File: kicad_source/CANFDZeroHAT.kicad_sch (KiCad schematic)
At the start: 34 parts, among them CN1 RASPI-IO, CN2 691322310004, CN3 GH_SM04B-GHS-TB, CN4 GH_SM04B-GHS-TB, SW1 JS202011JCQN, U1 MCP2518FD, U2 TCAN332GDR, Y1 RH100-40.000-18-F-2050-TR

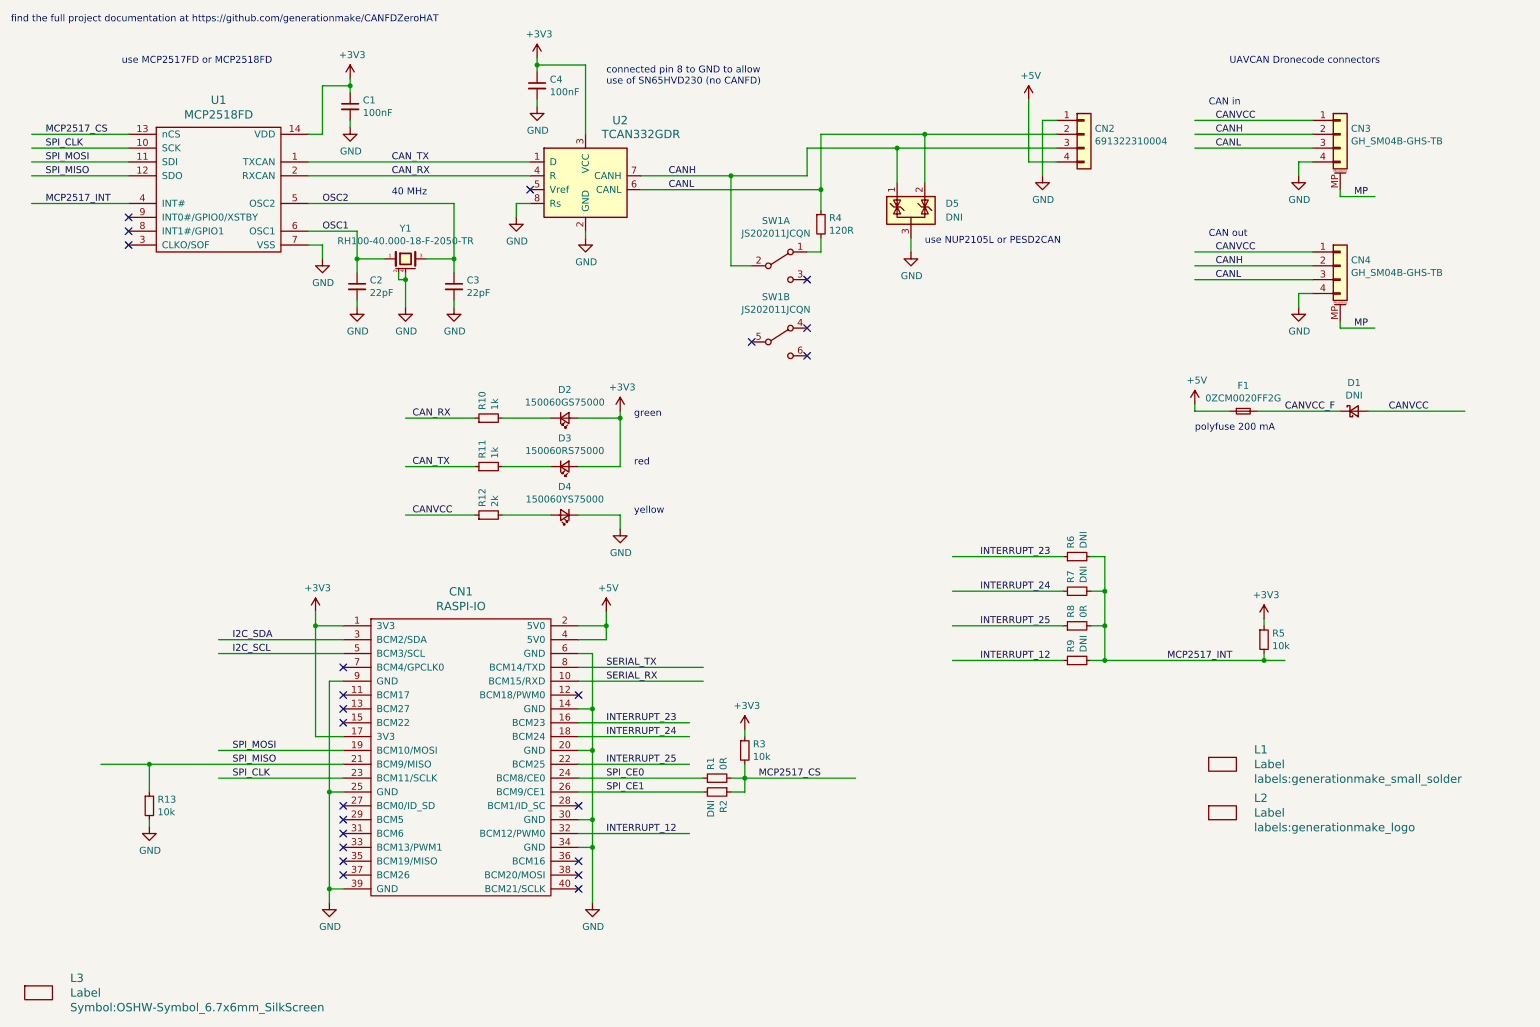
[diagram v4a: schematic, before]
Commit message: added some JLCPCB part numbers
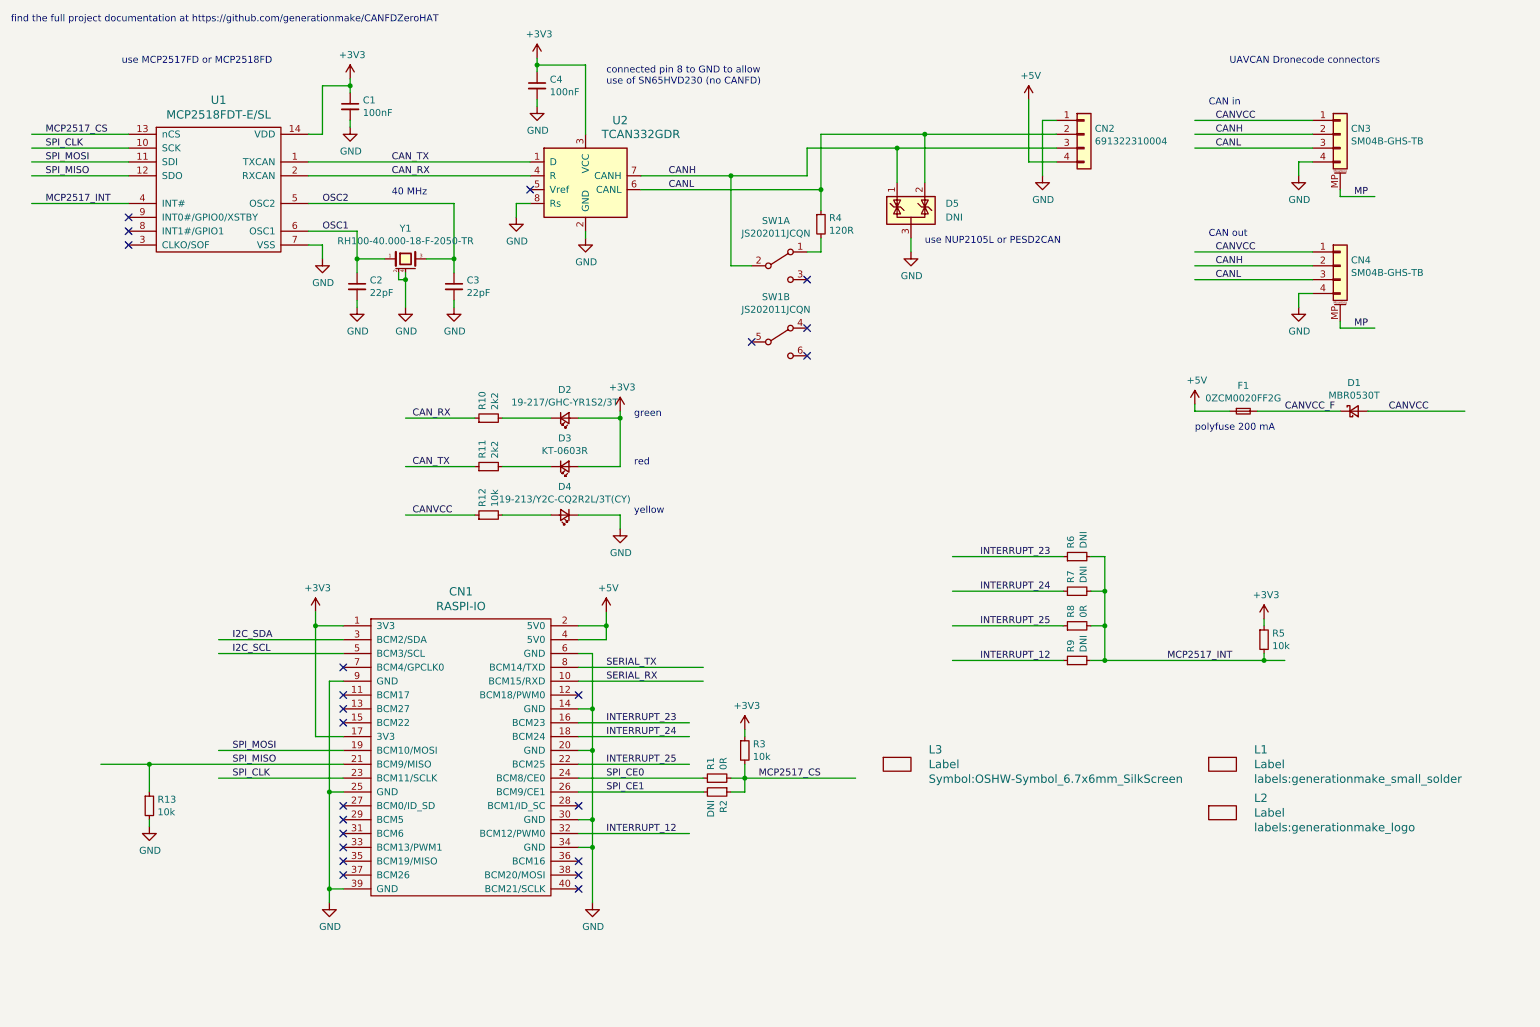
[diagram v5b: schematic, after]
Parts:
- C1, C4: LCSC (none) -> C14663
- C2, C3, D5, L1, L2, L3, R2, R6, R7, R9: now left out of the parts list
- CN3, CN4: value GH_SM04B-GHS-TB -> SM04B-GHS-TB; LCSC (none) -> C189895
- D1: value DNI -> MBR0530T; LCSC (none) -> C77336
- D2: value 150060GS75000 -> 19-217/GHC-YR1S2/3T; LCSC (none) -> C72043
- D3: value 150060RS75000 -> KT-0603R; LCSC (none) -> C2286
- D4: value 150060YS75000 -> 19-213/Y2C-CQ2R2L/3T(CY); LCSC (none) -> C72038
- R1, R8: LCSC (none) -> C2889381
- R10, R11: value 1k -> 2k2; LCSC (none) -> C4190
- R12: value 2k -> 10k; LCSC (none) -> C25804
- R13, R3, R5: LCSC (none) -> C25804
- R4: LCSC (none) -> C22787
- U1: value MCP2518FD -> MCP2518FDT-E/SL; LCSC (none) -> C626758
- U2: LCSC (none) -> C191010
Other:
- moved on the sheet: L3

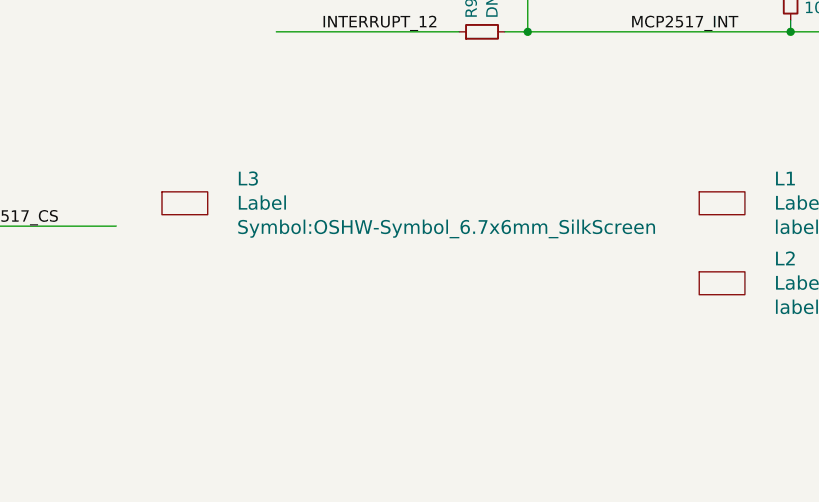
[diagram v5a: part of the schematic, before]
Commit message: added cyphal logo
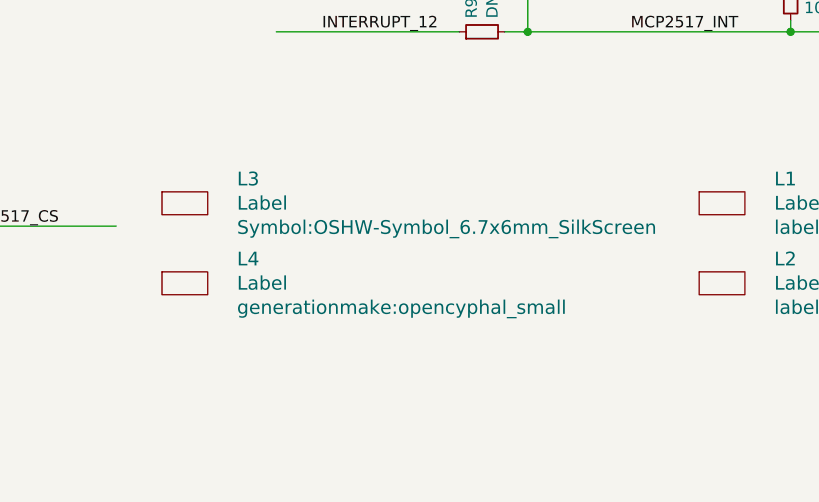
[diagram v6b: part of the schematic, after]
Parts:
- added L4: Label, generationmake:opencyphal_small, symbol generationmake:Label
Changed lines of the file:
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@@
   (title_block
     (title "CANFDZeroHAT")
-    (date "2023-08-24")
+    (date "2023-08-27")
     (rev "0.3")
     (company "generationmake")
@@
     (pin "2")
   )
+  (symbol (lib_id "generationmake:Label") (at 175.26 160.02 0) (unit 1)
+    (in_bom no) (on_board yes)
+    (property "Reference" "L4" (id 0) (at 181.0512 157.3276 0)
+      (effects (font (size 1.524 1.524)) (justify left))
+    )
+    (property "Value" "Label" (id 1) (at 181.0512 160.02 0)
+      (effects (font (size 1.524 1.524)) (justify left))
+    )
+    (property "Footprint" "generationmake:opencyphal_small" (id 2) (at 181.0512 162.7124 0)
+      (effects (font (size 1.524 1.524)) (justify left))
+    )
+    (property "Datasheet" "" (id 3) (at 175.26 160.02 0)
+      (effects (font (size 1.524 1.524)))
+    )
+  )
   (symbol (lib_id "Switch:SW_DPDT_x2") (at 153.67 73.66 0) (unit 2)
     (in_bom yes) (on_board yes)
@@
       (reference "L3") (unit 1) (value "Label") (footprint "Symbol:OSHW-Symbol_6.7x6mm_SilkScreen")
     )
+    (path "/c90de6ec-8b1e-4482-a692-291e6d522cdb"
+      (reference "L4") (unit 1) (value "Label") (footprint "generationmake:opencyphal_small")
+    )
     (path "/00000000-0000-0000-0000-00005fd836f1"

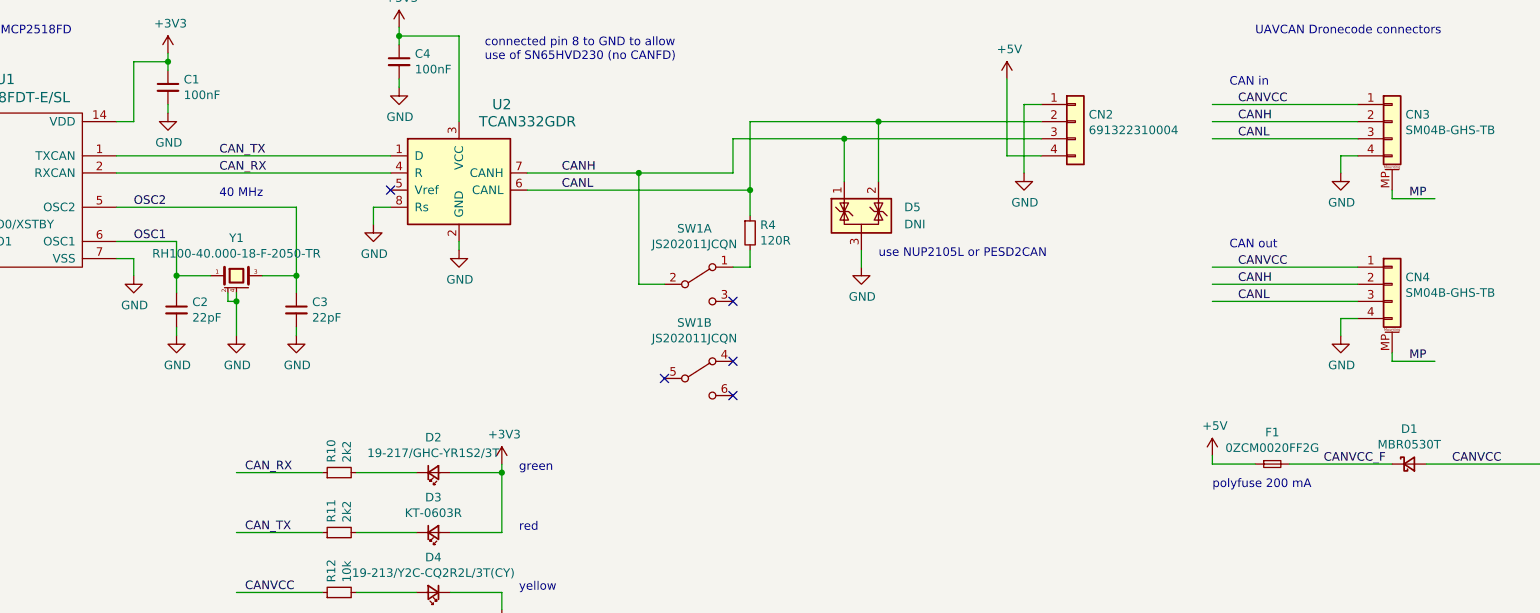
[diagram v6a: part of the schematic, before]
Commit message: updated some part numbers
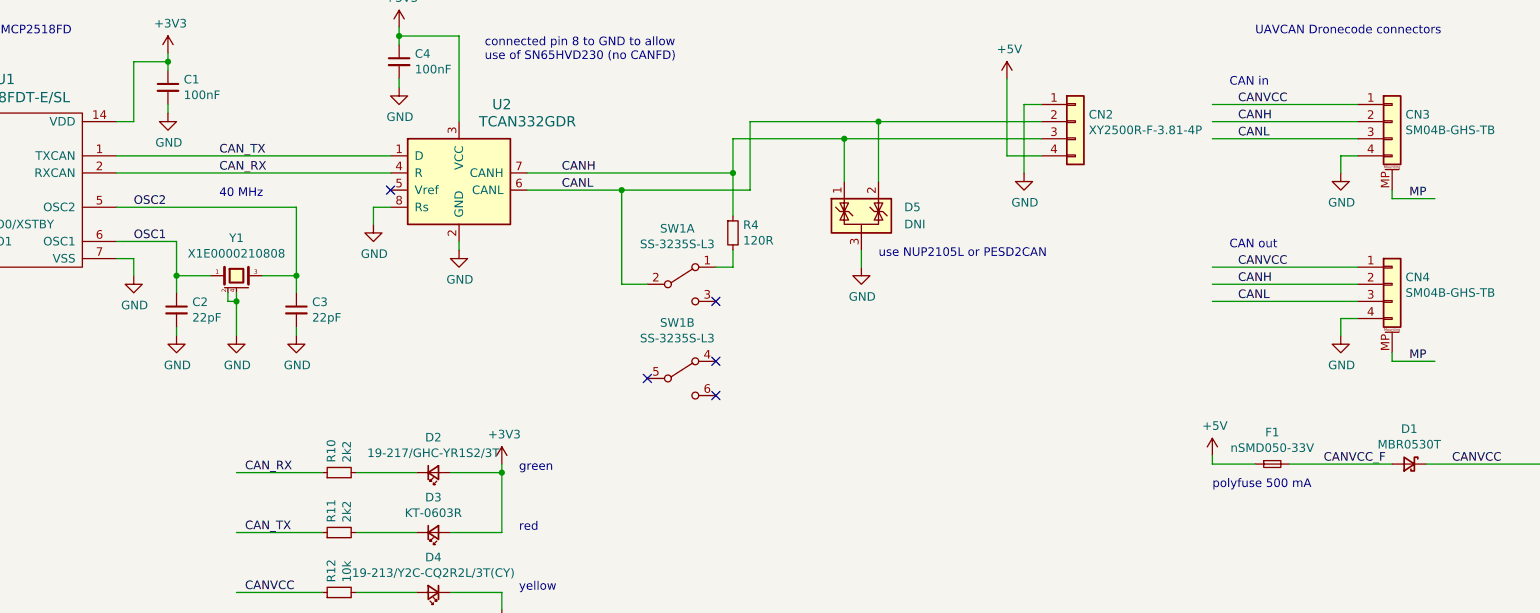
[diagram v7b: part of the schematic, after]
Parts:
- CN2: value 691322310004 -> XY2500R-F-3.81-4P; footprint CON_wuerth:WR-TBL_691322310004 -> Connector_Phoenix_MC:PhoenixContact_MC_1,5_4-G-3.81_1x04_P3.81mm_Horizontal; LCSC (none) -> C880583
- F1: value 0ZCM0020FF2G -> nSMD050-33V; footprint Resistor_SMD:R_0603_1608Metric -> Fuse:Fuse_1206_3216Metric; LCSC (none) -> C70077
- SW1: value JS202011JCQN -> SS-3235S-L3; footprint mechanical-switches:CK_JS202011JCQN -> generationmake:SW_DPDT_XKB_SS-3235S-L3; LCSC (none) -> C381098
- Y1: value RH100-40.000-18-F-2050-TR -> X1E0000210808; footprint crystals:Crystal_SMD_3.2x2.5mm_4Pad -> Crystal:Crystal_SMD_3225-4Pin_3.2x2.5mm; LCSC (none) -> C255941
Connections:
- net CANH: now also R4.1; no longer SW1.2 (B)
- net CANL: now also SW1.2 (B); no longer R4.1
- net CANVCC: now also D1.1 (K); no longer D1.2 (A)
- net CANVCC_F: now also D1.2 (A); no longer D1.1 (K)
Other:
- note added: "polyfuse 500 mA"
- note removed: "polyfuse 200 mA"
- moved on the sheet: R4, SW1A, SW1B

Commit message: added one JLCPCB part number
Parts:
- CN1: LCSC (none) -> C50982
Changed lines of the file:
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@@
       (effects (font (size 1.524 1.524)))
+    )
+    (property "LCSC" "C50982" (id 4) (at 95.25 149.86 0)
+      (effects (font (size 1.27 1.27)) hide)
     )
     (pin "1")
